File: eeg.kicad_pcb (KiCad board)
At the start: 2 copper layers, 80.3 x 46.1 mm, 126 parts, among them J1 USB_B_Mini, U10 -.+2.5V.+3.3V-GND, U11 +5V, U12 RN4678-V_RM100, U4 TPS73133DBV, U5 TPS73115DBV, U6 TPS60151DRV, U61 Electrode2, U7 DATA, U8 Electrode1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

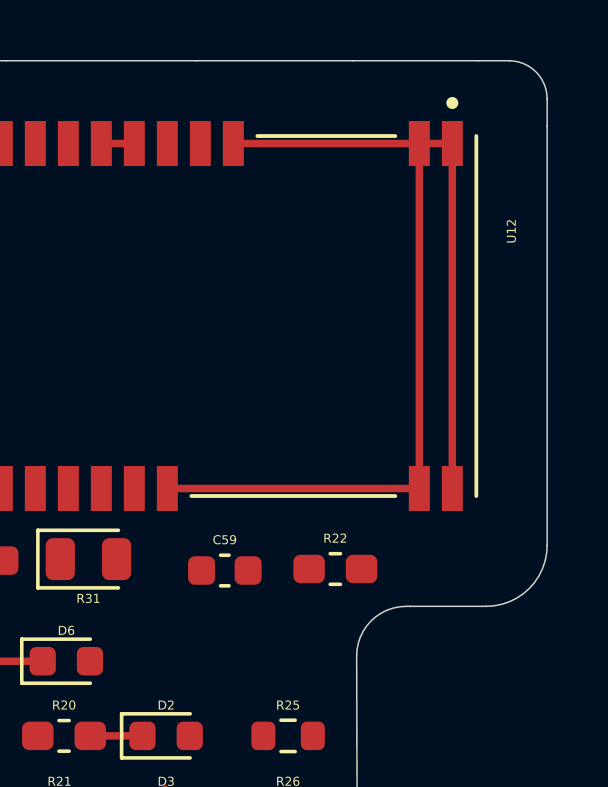
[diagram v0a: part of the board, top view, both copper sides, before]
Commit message: RN4678 3D view added
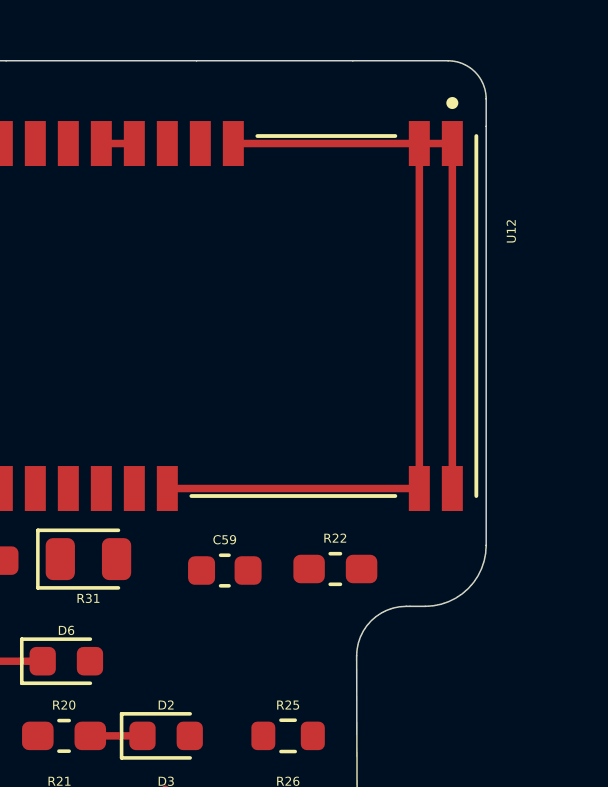
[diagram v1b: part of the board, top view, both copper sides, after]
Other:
- board size 80.3 x 46.1 mm -> 78.3 x 46.1 mm

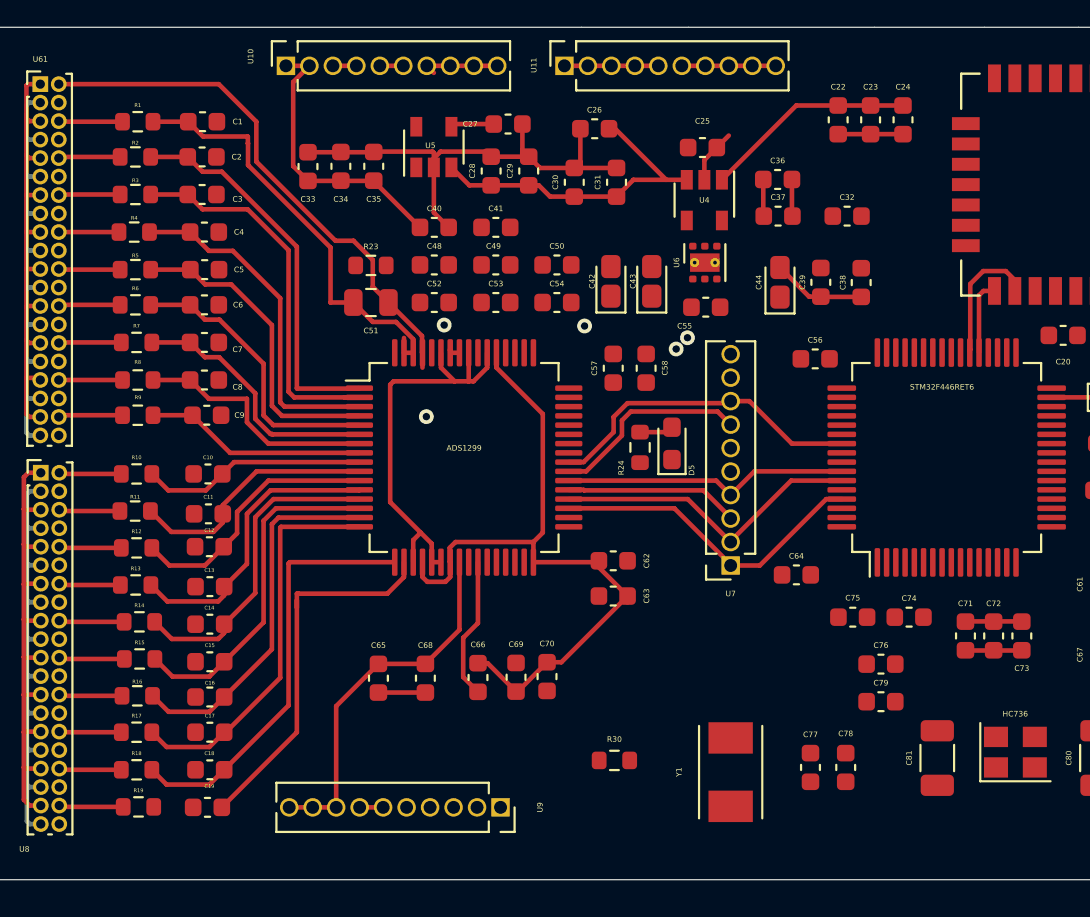
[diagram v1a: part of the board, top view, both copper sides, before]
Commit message: ERA-3A FOOTPRINT ADDED
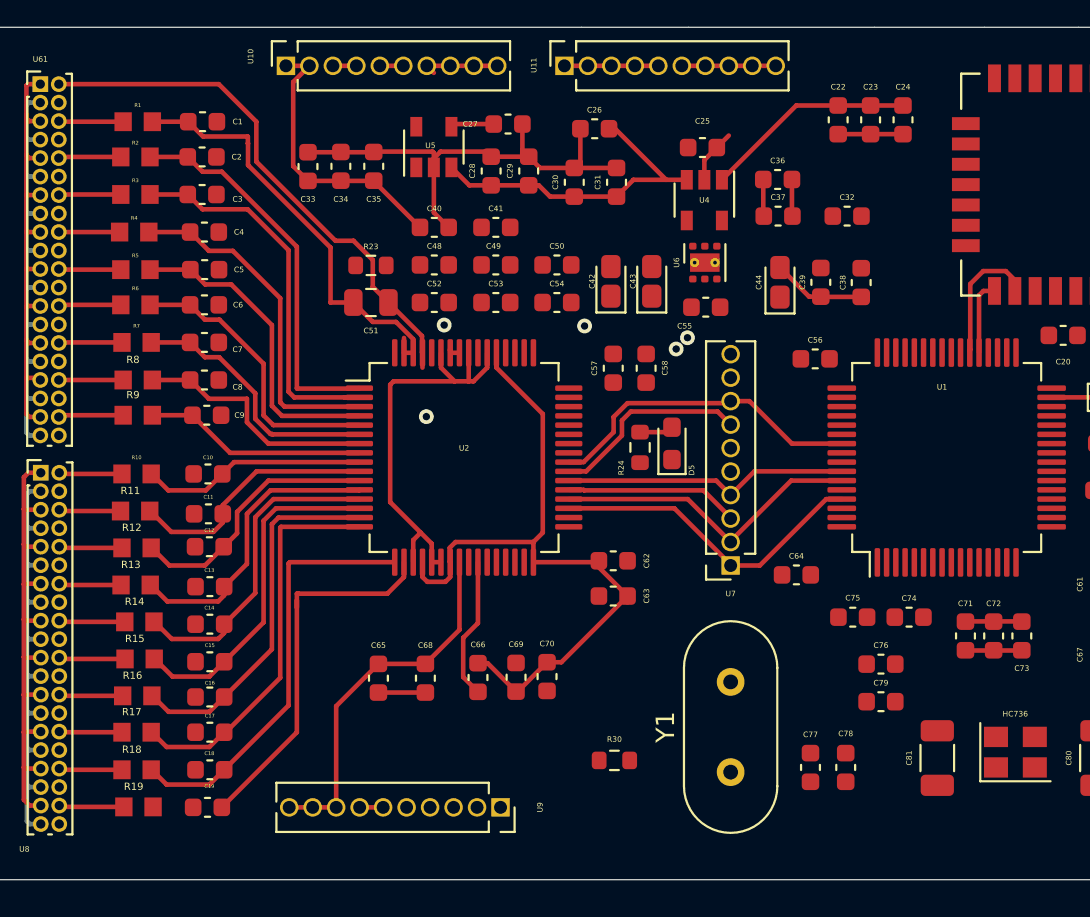
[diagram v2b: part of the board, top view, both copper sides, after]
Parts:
- R1, R10, R11, R12, R13, R14, R15, R16, R17, R18, R19, R2, R3, R4, R5, R6, R7, R8, R9: footprint Resistor_SMD:R_0603_1608Metric -> ERA-3A:RESC1608X55N
- Y1: footprint Crystal:Crystal_SMD_TXC_7A-2Pin_5x3.2mm -> Crystal:Crystal_HC49-4H_Vertical
- renumbered STM32F446RET6 to U1, ADS1299 to U2

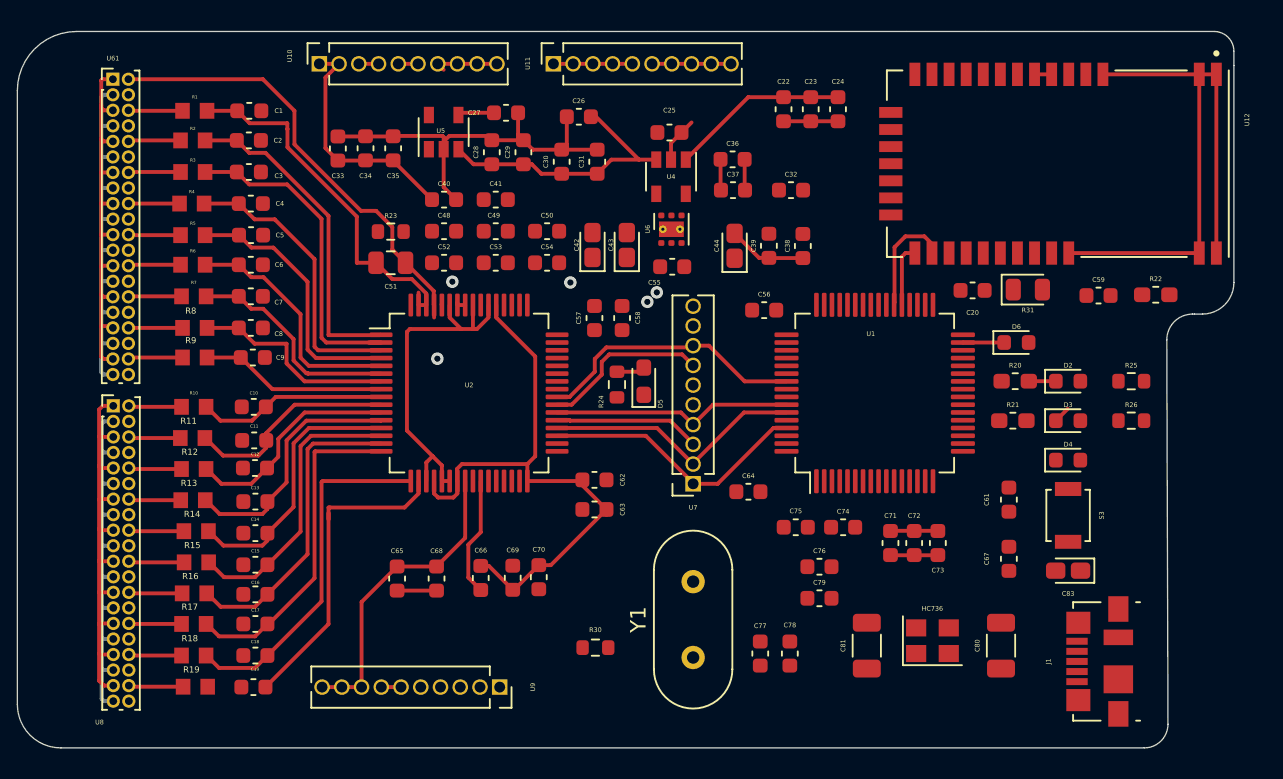
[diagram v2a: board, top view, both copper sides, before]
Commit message: Voltage Regulator Connection Fixed
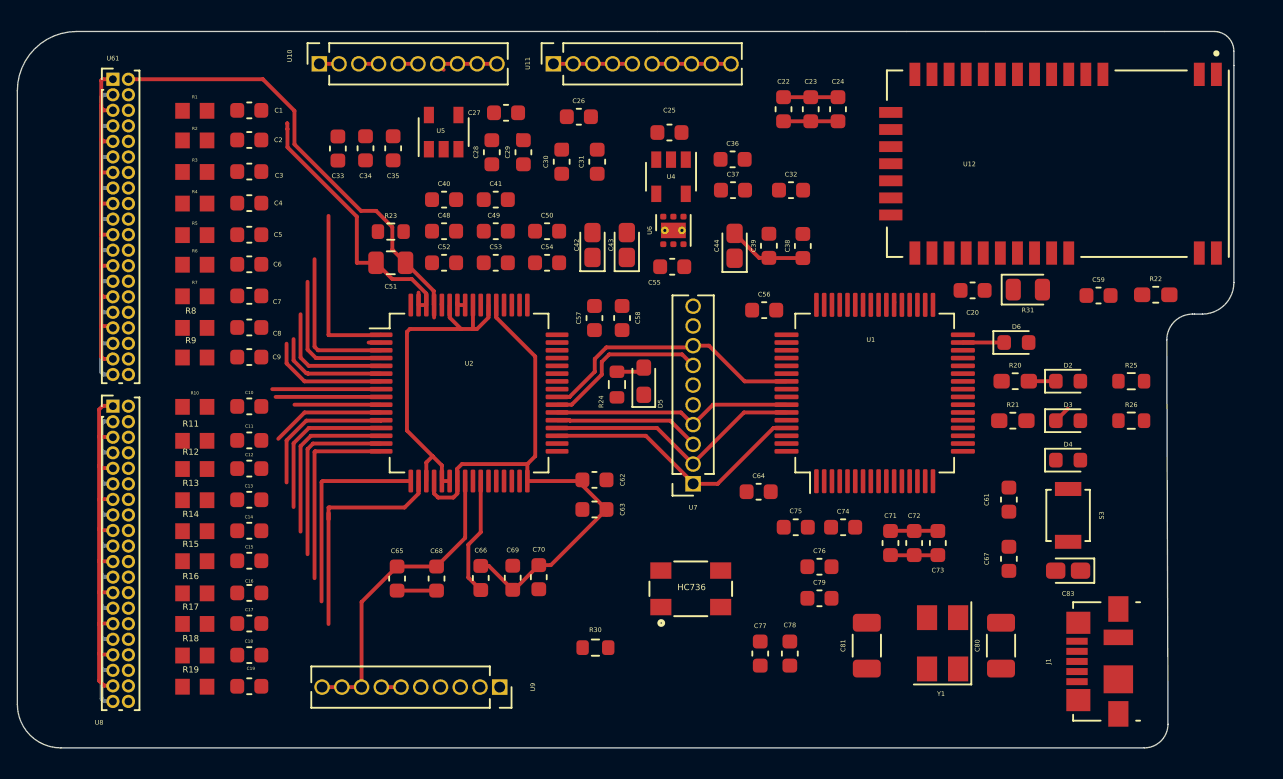
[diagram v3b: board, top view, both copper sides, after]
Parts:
- HC736: footprint Oscillator:Oscillator_SMD_Abracon_ASE-4Pin_3.2x2.5mm -> ERA-3A:OSCCC500X320X150N
- Y1: footprint Crystal:Crystal_HC49-4H_Vertical -> Crystal:Crystal_SMD_5032-4Pin_5.0x3.2mm
- moved Y1 16.1 mm to (94.8, 87.2)
- moved HC736 15.9 mm to (78.6, 83.7), turned to 90 degrees
- moved C64 0.66 mm to (83.0, 77.5)
- moved C15 0.47 mm to (50.2, 81.9)
- moved C14 0.42 mm to (50.2, 80.0)
- moved C13 0.41 mm to (50.2, 78.0)
- moved C16 0.40 mm to (50.2, 84.0)
- moved C17 0.39 mm to (50.2, 86.0)
- moved C18 0.39 mm to (50.2, 88.0)
- moved C12 0.37 mm to (50.2, 76.0)
- moved C11 0.32 mm to (50.2, 74.2)
- moved C10 0.29 mm to (50.2, 72.0)
- moved C19 0.27 mm to (50.2, 90.0)
- moved C9 0.23 mm to (50.2, 68.8)
- moved R11 0.23 mm to (46.7, 74.2)
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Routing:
- net GNDREF: track 45.7 -> 6.97 mm
- net GND: track 42.2 -> 14.4 mm
- net +5V: track 34.8 -> 9.19 mm
- net /IN8P: track 21.1 -> 0.80 mm
- net +2V5: track 37.9 -> 23.9 mm
- net /IN8N: track 21.0 -> 11.1 mm
- net /SRB1: track 22.9 -> 13.4 mm
- net /IN1P: track 21.2 -> 12.4 mm
- net /IN7N: track 18.6 -> 10.0 mm
- net /IN1N: track 19.9 -> 11.6 mm
- net /IN4P: track 13.7 -> 5.56 mm
- net /IN7P: track 17.1 -> 9.32 mm
- net /IN2P: track 18.4 -> 11.0 mm
- net /IN6N: track 15.6 -> 8.19 mm
- net /IN2N: track 17.3 -> 10.1 mm
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
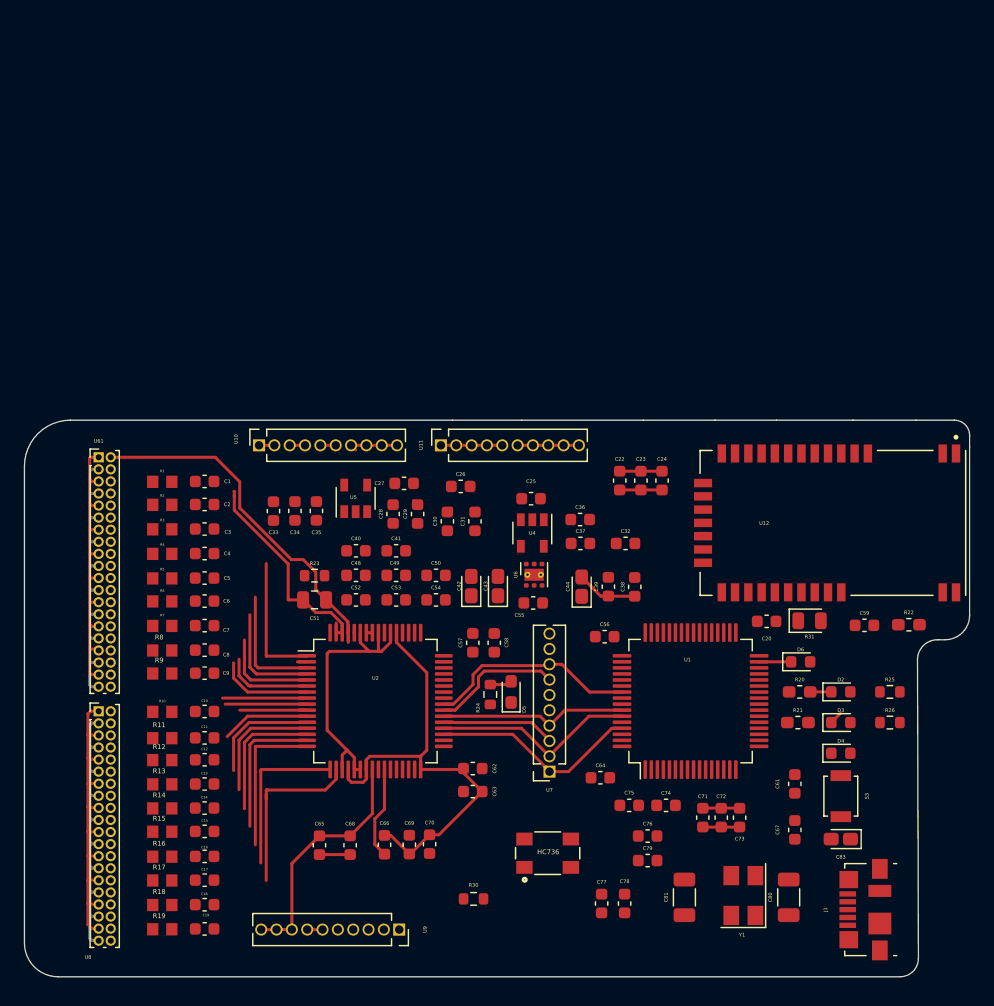
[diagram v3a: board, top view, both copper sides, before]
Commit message: Added capacitor footprints redrawed voltage regulators
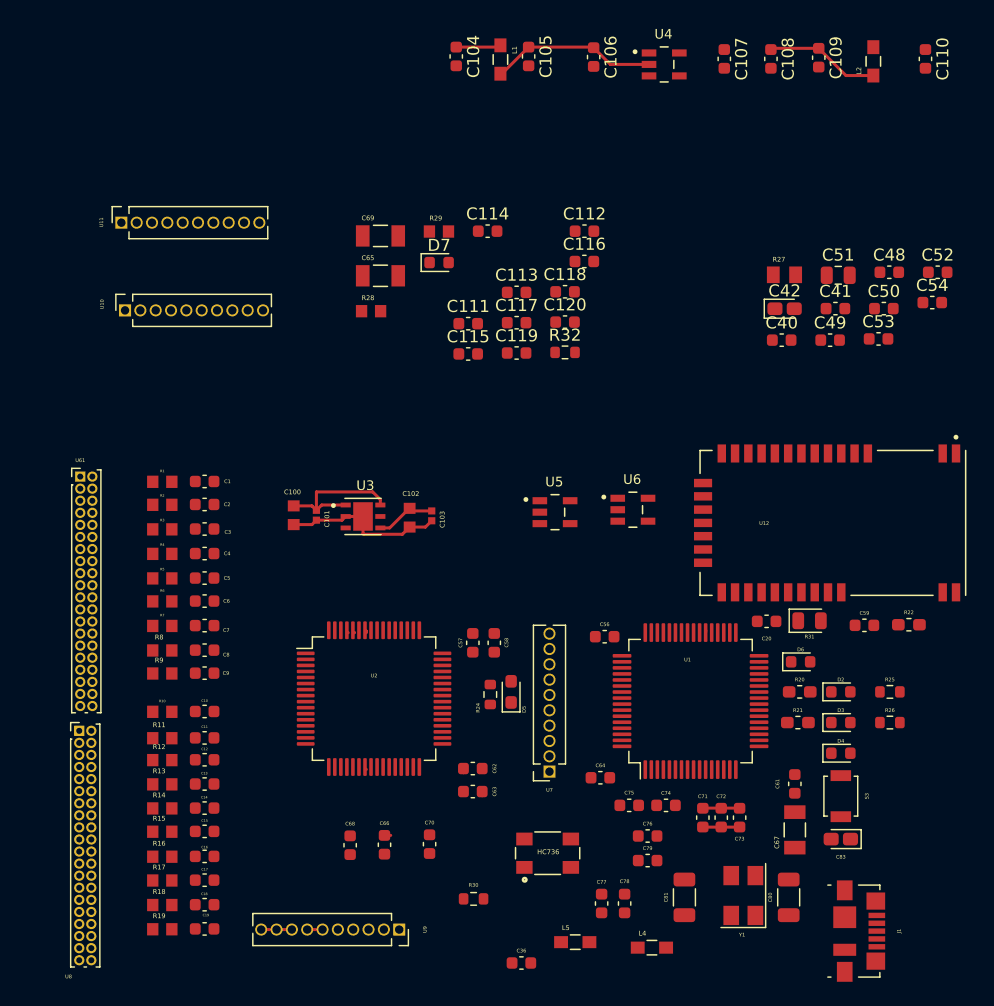
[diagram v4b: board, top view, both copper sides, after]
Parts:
- removed C22, C25, C27, C28, C31, C32, C35, C37, C55: 1uF, Capacitor_SMD:C_0603_1608Metric
- removed C23, C24, C26, C29, C30, C33, C39: 10uF, Capacitor_SMD:C_0603_1608Metric
- removed C34, C38: 2.2uF, Capacitor_SMD:C_0603_1608Metric
- removed C43, C44: 0.1uF, Capacitor_Tantalum_SMD:CP_EIA-1608-08_AVX-J_Pad1.25x1.05mm_HandSolder
- removed R23: 210K, Resistor_SMD:R_0603_1608Metric
- added C100: 1uF_X5R_0603, 06033D105KAT2A:CAPC1608X94N, F.Cu at (57.6, 55.7)
- added C101: 100nF, C0402C104K4RACTU:CAPC1005X55N, F.Cu at (59.4, 55.7)
- added C102: 1uF_X5R_0603, 06033D105KAT2A:CAPC1608X94N, F.Cu at (67.2, 55.9)
- added C103: 100nF, C0402C104K4RACTU:CAPC1005X55N, F.Cu at (69.0, 55.8)
- added C104: 10uF, Capacitor_SMD:C_0603_1608Metric, F.Cu at (71.0, 17.7)
- added C105: 10uF, Capacitor_SMD:C_0603_1608Metric, F.Cu at (77.0, 17.7)
- added C106: 1uF, Capacitor_SMD:C_0603_1608Metric, F.Cu at (82.4, 17.8)
- added C107: 1uF, Capacitor_SMD:C_0603_1608Metric, F.Cu at (93.2, 17.9)
- added C108: 1uF, Capacitor_SMD:C_0603_1608Metric, F.Cu at (97.1, 17.9)
- added C109: 10uF, Capacitor_SMD:C_0603_1608Metric, F.Cu at (101.0, 17.8)
- added C110: 10uF, Capacitor_SMD:C_0603_1608Metric, F.Cu at (109.9, 17.9)
- added C111: 1uF, Capacitor_SMD:C_0603_1608Metric, F.Cu at (72.0, 39.9)
- added C112: 1uF, Capacitor_SMD:C_0603_1608Metric, F.Cu at (81.6, 32.2)
- added C113: 2.2uF, Capacitor_SMD:C_0603_1608Metric, F.Cu at (76.0, 37.3)
- added C114: 10uF, Capacitor_SMD:C_0603_1608Metric, F.Cu at (73.6, 32.2)
- added C115: 10uF, Capacitor_SMD:C_0603_1608Metric, F.Cu at (72.0, 42.4)
- added C116: 2.2uF, Capacitor_SMD:C_0603_1608Metric, F.Cu at (81.6, 34.7)
- added C117: 0.01uF, Capacitor_SMD:C_0603_1608Metric, F.Cu at (76.0, 39.8)
- added C118: 2.2uF, Capacitor_SMD:C_0603_1608Metric, F.Cu at (80.0, 37.2)
- added C119: 10uF, Capacitor_SMD:C_0603_1608Metric, F.Cu at (76.0, 42.3)
- added C120: 10uF, Capacitor_SMD:C_0603_1608Metric, F.Cu at (80.0, 39.7)
- added D7: LED, LED_SMD:LED_0603_1608Metric, F.Cu at (69.6, 34.8)
- added L1: 3.3uH, MLZ2012A3R3WT000:INDC2012X87N, F.Cu at (74.7, 18.0)
- added L2: 3.3uH, MLZ2012A3R3WT000:INDC2012X87N, F.Cu at (105.6, 18.1)
- added L4: 3.3uH, MLZ2012A3R3WT000:INDC2012X87N, F.Cu at (87.2, 91.5)
- added L5: 3.3uH, MLZ2012A3R3WT000:INDC2012X87N, F.Cu at (80.9, 91.1)
- added R27: 1M, ERA-6AEB105V:RESC2012X60N, F.Cu at (98.2, 35.8)
- added R28: 10K, ERA-3A:RESC1608X55N, F.Cu at (64.0, 38.8)
- added R29: 10K, ERA-3A:RESC1608X55N, F.Cu at (69.6, 32.2)
- added R32: 270, Resistor_SMD:R_0603_1608Metric, F.Cu at (80.0, 42.2)
- added U3: LD39050PU33R, LD39050PU33R:SON95P300X300X100-7N, F.Cu at (63.3, 55.8)
- C65, C67, C69: footprint Capacitor_SMD:C_0603_1608Metric -> TCA1C106M8R:RESC3216X65N
- U4: value TPS73133DBV -> TPS60403DBVT; footprint Package_TO_SOT_SMD:SOT-23-5 -> SOT95P280X145-5N
- U5: value TPS73115DBV -> TPS73225DBVT; footprint Package_TO_SOT_SMD:SOT-23-5 -> SOT95P280X145-5N
- U6: value TPS60151DRV -> TPS72325DBVT; footprint Package_SON:WSON-6-1EP_2x2mm_P0.65mm_EP1x1.6mm_ThermalVias -> SOT95P280X145-5N
- moved C52 55.3 mm to (110.9, 35.6)
- moved C51 51.0 mm to (102.7, 35.9), turned to 0 degrees
- moved C48 50.8 mm to (106.9, 35.6)
- moved C69 50.5 mm to (64.7, 32.6), turned to 0 degrees
- moved C54 47.9 mm to (110.4, 38.1)
- moved C65 47.4 mm to (64.7, 35.9), turned to 0 degrees
- moved C53 45.4 mm to (106.0, 41.1)
- moved C50 43.2 mm to (106.4, 38.6)
- moved C41 41.5 mm to (102.4, 38.6)
- moved C49 40.9 mm to (102.0, 41.2)
- moved U4 40.3 mm to (88.2, 18.4), turned to 0 degrees
- moved C40 39.3 mm to (98.0, 41.2)
- moved C36 37.0 mm to (76.4, 92.8)
- moved C42 34.7 mm to (98.2, 38.6), turned to 0 degrees
- moved U11 32.3 mm to (43.3, 31.5)
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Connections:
- net Net-(U1-Pad15) renamed /RN46CTS
- C65 pad 1: /-2.5V -> /VREFP
- C65 pad 2: /VREFP -> /-2.5V
- C69 pad 1: -2V5 -> Net-(C69-Pad1)
- C69 pad 2: Net-(C69-Pad2) -> -2V5
- U1 pad 14: Net-(U1-Pad14) -> /RN46RTS
- U2 pad 28: Net-(C69-Pad2) -> Net-(C69-Pad1)
- U4 pad 1: +5V -> Net-(C108-Pad1)
- U4 pad 2: GND -> Net-(C105-Pad1)
- U4 pad 3: +5V -> Net-(C107-Pad2)
- U4 pad 4: Net-(C32-Pad1) -> GND
- U4 pad 5: +3V3 -> Net-(C107-Pad1)
- U5 pad 1: +5V -> Net-(C105-Pad1)
- U5 pad 3: +5V -> Net-(C105-Pad1)
- U6 pad 2: +5V -> -5V
- U6 pad 3: /-5v_UNREG -> -5V
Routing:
- net /-2.5V: track 53.9 -> 0.00 mm
- net /+2.5V: track 52.8 -> 0.00 mm
- net -2V5: track 40.7 -> 1.54 mm
- net /BIASINV: track 29.1 -> 0.04 mm
- net +2V5: track 23.9 -> 0.00 mm
- net /BIASIN: track 18.2 -> 0.00 mm
- net PWDN: track 17.6 -> 0.05 mm
- net /VREFP: track 20.1 -> 2.54 mm
- net SCLK: track 17.7 -> 0.31 mm
- net RESET: track 17.1 -> 0.05 mm
- net START: track 15.6 -> 0.00 mm
- net /SRB2: track 14.9 -> 0.00 mm
- net GND: track 14.4 -> 0.05 mm
- net Net-(C105-Pad1): track 0.00 -> 13.8 mm
- net Net-(C100-Pad2): track 0.00 -> 13.6 mm
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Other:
- board outline removed
